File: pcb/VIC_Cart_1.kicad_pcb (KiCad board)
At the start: 2 copper layers, 126.5 x 77.3 mm, 30 parts, among them J1 VIC-20_Expansion_Port, J2 I2C Display, SW1 SW_Push, SW2 SW_Push, SW3 SW_Push, U1 ATMEGA328P-PU, U2 KM681000CLG-5L, U3 M27C160, U4 74LS148, U5 74LS21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

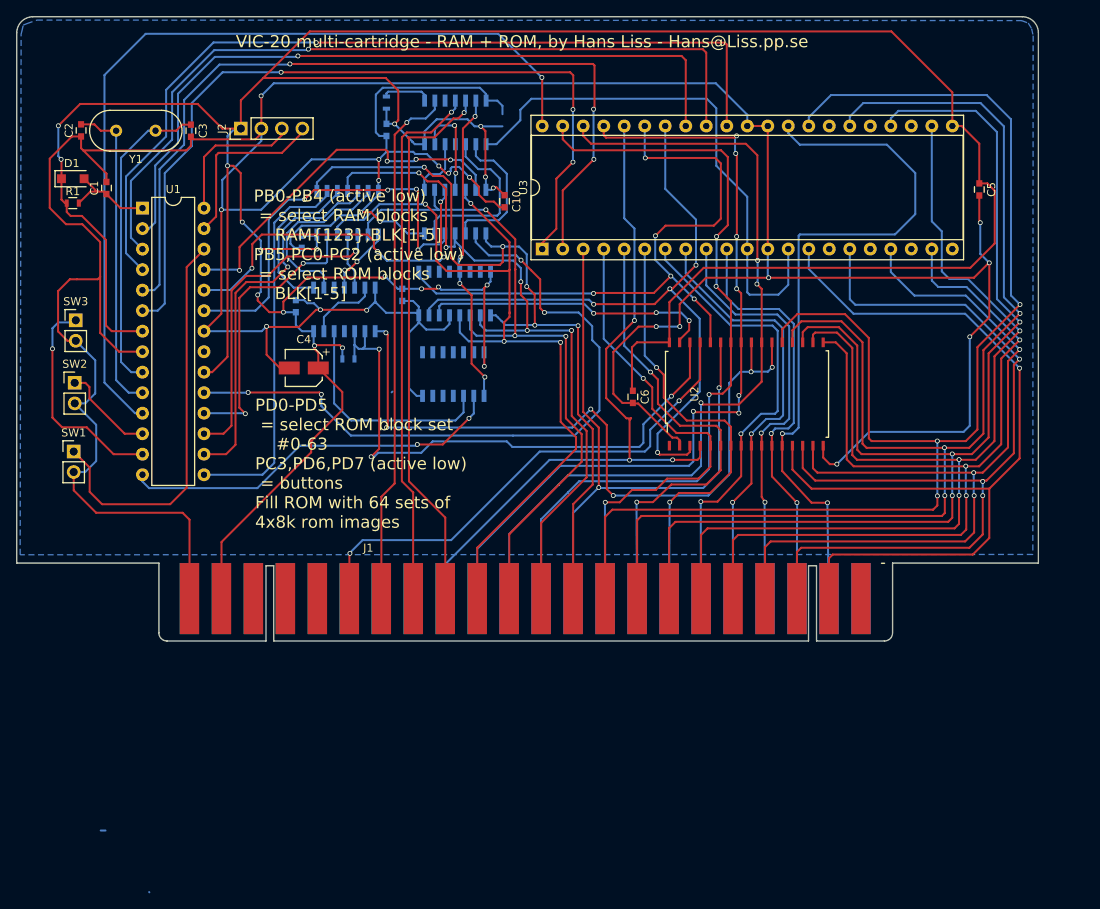
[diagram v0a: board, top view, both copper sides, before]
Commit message: Changed pads to pin header footprint for buttons Inverted BLK inputs to encoder to correct addressing error Added component values to silkscreen
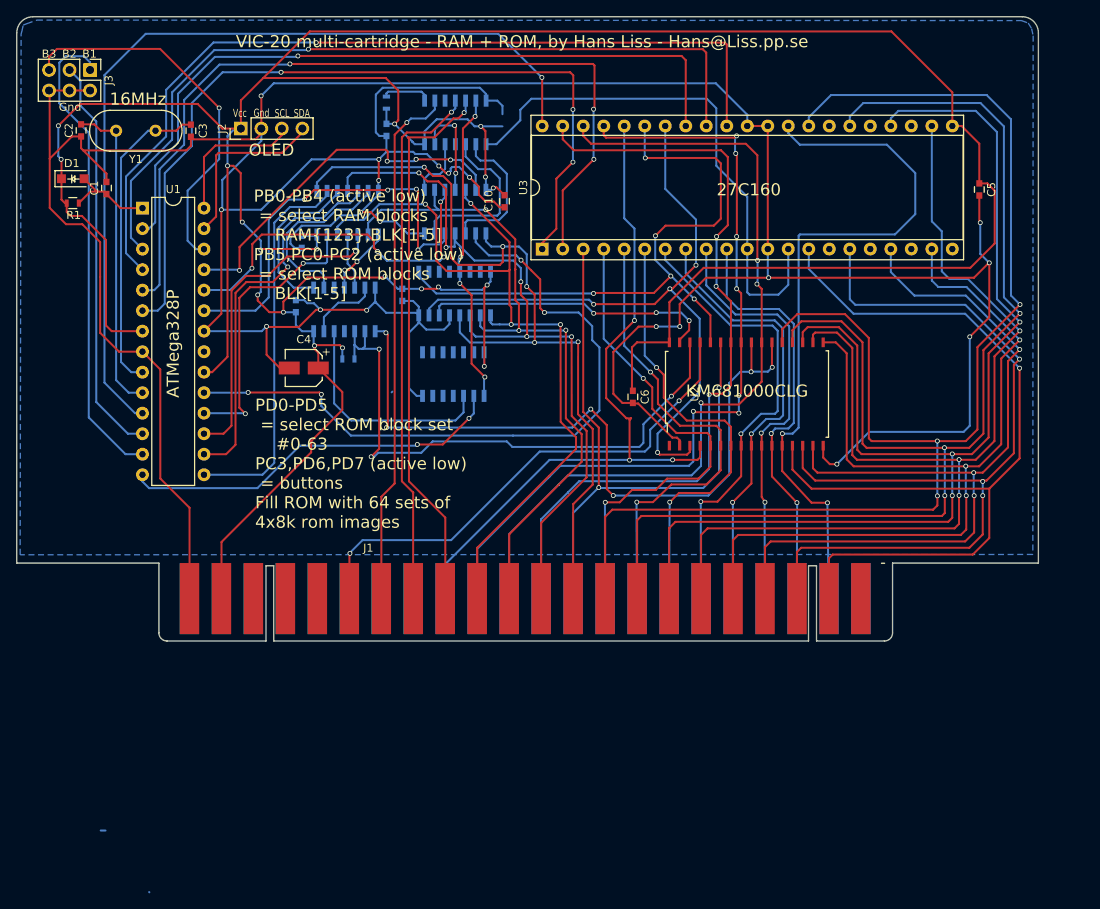
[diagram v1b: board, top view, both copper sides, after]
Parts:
- removed SW1, SW2, SW3: SW_Push, Pin_Headers:Pin_Header_Straight_1x02_Pitch2.54mm
- added J3: Buttons, Pin_Headers:Pin_Header_Straight_2x03_Pitch2.54mm, F.Cu at (53.1, 38.8)
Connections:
- J1 pad 1: Net-(J1-Pad1) -> (no net)
- J1 pad 18: Net-(J1-Pad18) -> (no net)
- J1 pad 19: Net-(J1-Pad19) -> (no net)
- J1 pad 20: Net-(J1-Pad20) -> (no net)
- J1 pad A: Net-(J1-PadA) -> (no net)
- J1 pad S: Net-(J1-PadS) -> (no net)
- J1 pad T: Net-(J1-PadT) -> (no net)
- J1 pad U: Net-(J1-PadU) -> (no net)
- J1 pad V: Net-(J1-PadV) -> (no net)
- J1 pad W: Net-(J1-PadW) -> (no net)
- J1 pad X: Net-(J1-PadX) -> (no net)
- J1 pad Y: Net-(J1-PadY) -> (no net)
- J1 pad Z: Net-(J1-PadZ) -> (no net)
- U1 pad 21: Net-(U1-Pad21) -> (no net)
- U2 pad 1: Net-(U2-Pad1) -> (no net)
- U3 pad 15: Net-(U3-Pad15) -> (no net)
- U3 pad 17: Net-(U3-Pad17) -> (no net)
- U3 pad 19: Net-(U3-Pad19) -> (no net)
- U3 pad 21: Net-(U3-Pad21) -> (no net)
- U3 pad 24: Net-(U3-Pad24) -> (no net)
- U3 pad 26: Net-(U3-Pad26) -> (no net)
- U3 pad 28: Net-(U3-Pad28) -> (no net)
- U4 pad 1: /~BLK1 -> /~BLK5
- U4 pad 10: Net-(U4-Pad10) -> (no net)
- U4 pad 11: Net-(U4-Pad11) -> (no net)
- U4 pad 12: Net-(U4-Pad12) -> (no net)
- U4 pad 14: Net-(U4-Pad14) -> (no net)
- U4 pad 15: Net-(U4-Pad15) -> (no net)
- U4 pad 2: /~BLK2 -> /~BLK3
- U4 pad 3: /~BLK3 -> /~BLK2
- U4 pad 4: /~BLK5 -> /~BLK1
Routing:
- net /~BUTTON2: track 11.8 -> 49.8 mm
- net /~BUTTON3: track 27.4 -> 59.4 mm, vias 1 -> 0
- net GND: track 530.1 -> 513.0 mm
- net /~BLK1: track 100.2 -> 106.2 mm
- net /~BLK5: track 104.3 -> 98.8 mm
- net /~BUTTON1: track 49.7 -> 46.8 mm, vias 0 -> 1
- net /~BLK2: track 92.6 -> 94.6 mm
- net /~BLK3: track 87.7 -> 86.0 mm
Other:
- board text added: "16MHz"
- board text added: "27C160"
- board text added: "74LS148"
- board text added: "74LS21"
- board text added: "74LS32"
- board text added: "ATMega328P"
- board text added: "B1"
- board text added: "B2"
- board text added: "B3"
- board text added: "Gnd"
- board text added: "KM681000CLG"
- board text added: "OLED"
- board text added: "SCL"
- board text added: "SDA"
- board text added: "Vcc"

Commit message: No change
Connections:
- J1 pad X: (no net) -> Net-(J1-PadX)
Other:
- board text added: "555"
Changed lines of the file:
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@@
     (area 43.924999 32.139799 170.615001 109.604881)
     (thickness 1.6)
-    (drawings 54)
-    (tracks 1526)
+    (drawings 55)
+    (tracks 1528)
     (zones 0)
     (modules 28)
-    (nets 73)
+    (nets 74)
   )
   (page A4)
@@
   (net 71 "Net-(U6-Pad13)")
   (net 72 "Net-(U6-Pad12)")
+  (net 73 "Net-(J1-PadX)")
   (net_class Default "This is the default net class."
     (clearance 0.2)
@@
     (add_net "Net-(J1-Pad15)")
     (add_net "Net-(J1-Pad16)")
+    (add_net "Net-(J1-PadX)")
     (add_net "Net-(R2-Pad2)")
     (add_net "Net-(R3-Pad2)")
@@
     (pad Z connect rect (at -83.12726 -0.71888) (size 2.4 8.8) (layers B.Cu B.Mask))
     (pad Y connect rect (at -79.16726 -0.71888) (size 2.4 8.8) (layers B.Cu B.Mask))
-    (pad X connect rect (at -75.20726 -0.71888) (size 2.4 8.8) (layers B.Cu B.Mask))
+    (pad X connect rect (at -75.20726 -0.71888) (size 2.4 8.8) (layers B.Cu B.Mask)
+      (net 73 "Net-(J1-PadX)"))
     (pad W connect rect (at -71.24726 -0.71888) (size 2.4 8.8) (layers B.Cu B.Mask))
     (pad V connect rect (at -67.28726 -0.71888) (size 2.4 8.8) (layers B.Cu B.Mask))
@@
       (rotate (xyz 0 0 0))
     )
+  )
+  (gr_text 555 (at 148.19 38.04 90) (layer B.SilkS)
+    (effects (font (size 1.5 1.5) (thickness 0.3)) (justify mirror))
   )
   (gr_line (start 50.82 52.32) (end 50.31 52.32) (angle 90) (layer F.SilkS) (width 0.05))
@@
   (segment (start 80.29956 34.03092) (end 74.53122 39.79926) (width 0.25) (layer F.Cu) (net 23))
   (segment (start 74.53122 39.79926) (end 71.755 42.57548) (width 0.25) (layer F.Cu) (net 23))
-  (segment (start 152.32888 34.03092) (end 80.29956 34.03092) (width 0.25) (layer F.Cu) (net 23))
-  (segment (start 159.8803 41.58234) (end 152.32888 34.03092) (width 0.25) (layer F.Cu) (net 23))
+  (segment (start 152.32888 34.03092) (end 145.29 34.03092) (width 0.25) (layer F.Cu) (net 23))
+  (segment (start 145.29 34.03092) (end 80.29956 34.03092) (width 0.25) (layer F.Cu) (net 23))
+  (segment (start 159.8803 41.58234) (end 152.85398 34.55602) (width 0.25) (layer F.Cu) (net 23))
+  (segment (start 152.85398 34.55602) (end 152.32888 34.03092) (width 0.25) (layer F.Cu) (net 23))
   (segment (start 79.2988 59.3464) (end 79.04156 59.3464) (width 0.25) (layer B.Cu) (net 23) (status 30))
   (segment (start 67.19062 76.2381) (end 68.199 76.2381) (width 0.25) (layer F.Cu) (net 23))

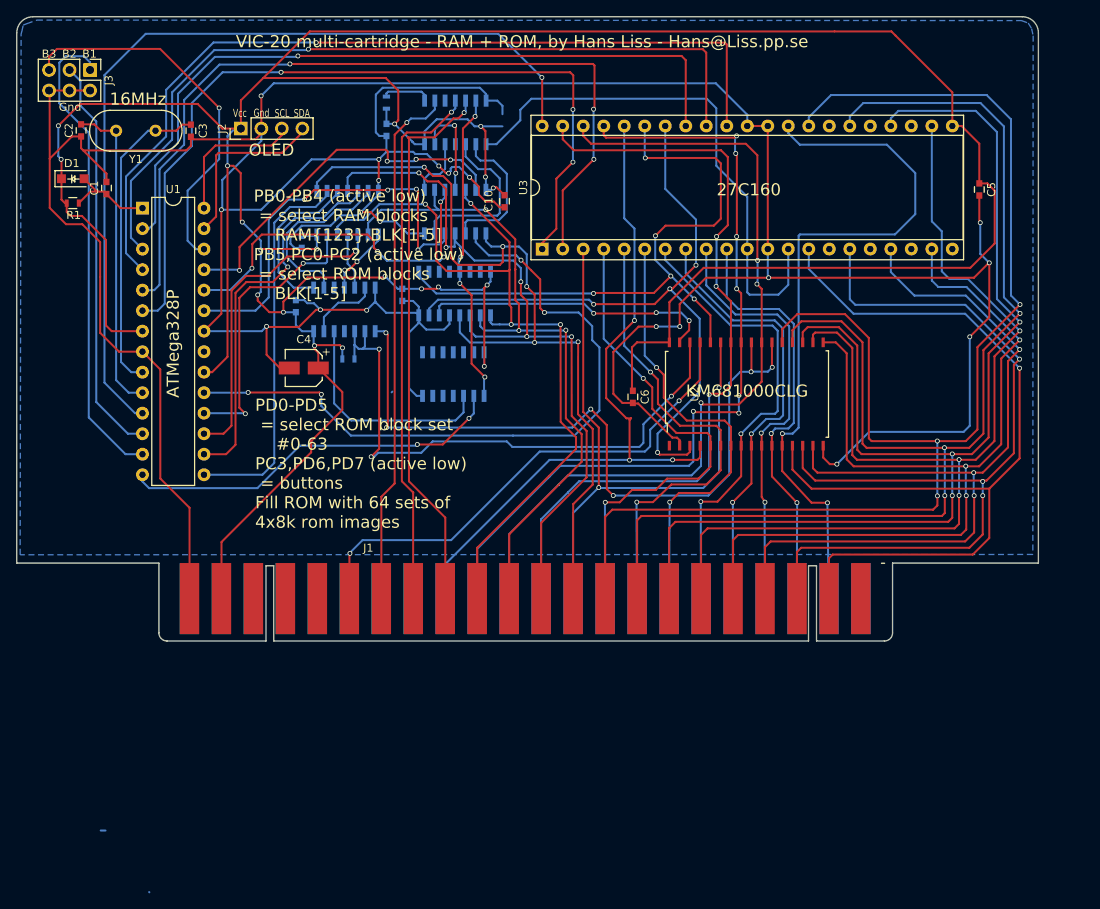
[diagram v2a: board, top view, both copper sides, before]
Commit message: Added mounting hole Added title
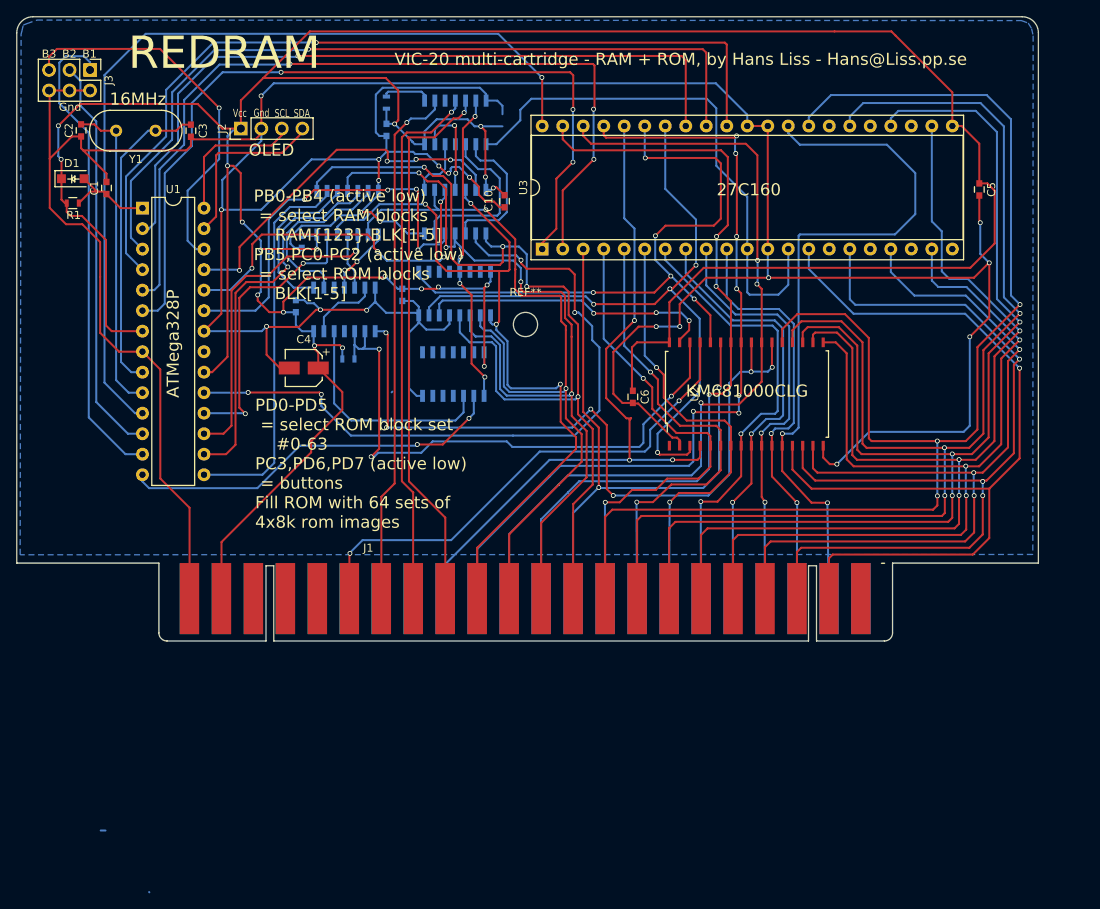
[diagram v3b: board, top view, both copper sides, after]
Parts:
- added REF**: MountingHole_3mm, Mounting_Holes:MountingHole_3mm, F.Cu at (107.0, 70.3)
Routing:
- net /~BLK3: track 86.0 -> 97.7 mm, vias 3 -> 2
- net /~BLK2: track 94.6 -> 106.0 mm, vias 5 -> 4
- net /~BLK1: track 106.2 -> 117.3 mm, vias 5 -> 4
- net /~SEL_ROM_BLK1: track 86.2 -> 87.1 mm
- net BA2: track 36.3 -> 36.9 mm
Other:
- board text added: "REDRAM"
- board text removed: "555"

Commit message: Moved button pin header to the right Changed outline to match existing (large) carts, e.g. 16k expansion
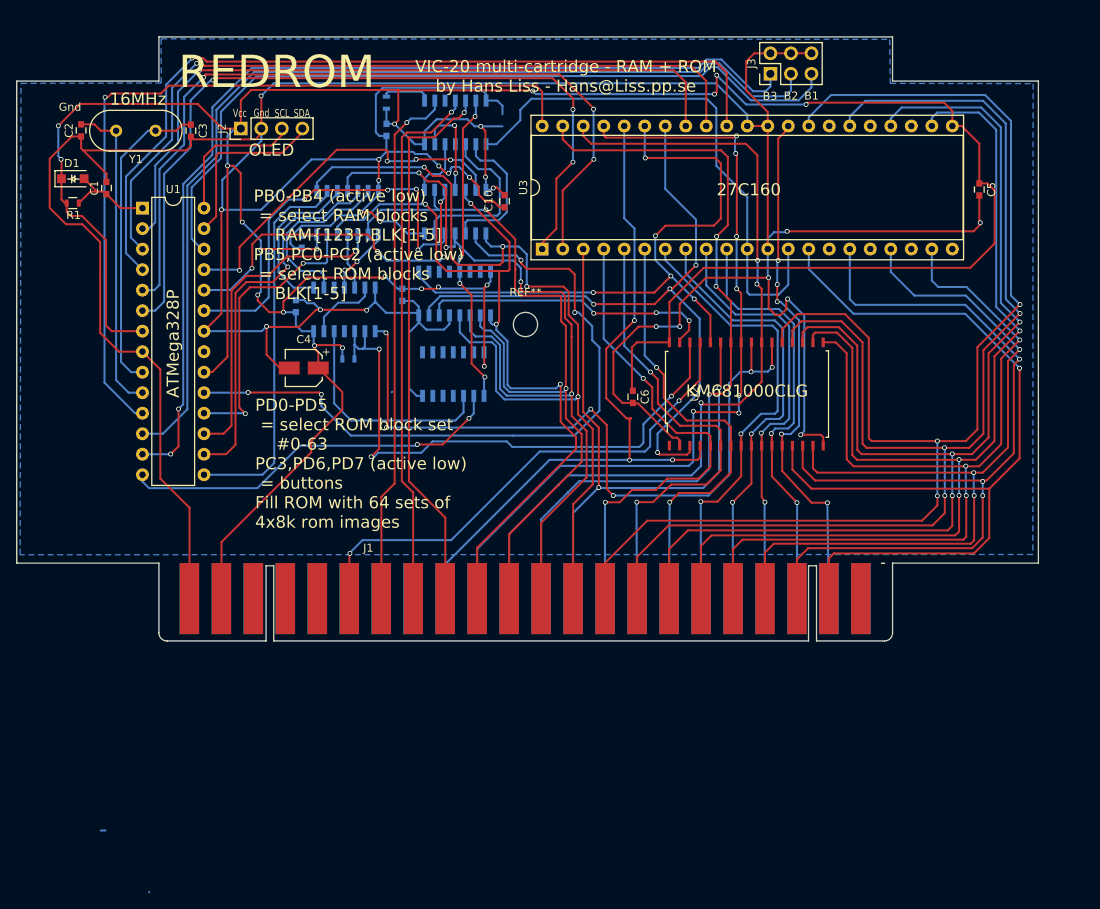
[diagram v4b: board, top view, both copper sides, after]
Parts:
- moved J3 84.3 mm to (137.3, 39.3), turned to 90 degrees
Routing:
- net /~BUTTON2: track 49.8 -> 123.0 mm
- net /~BUTTON3: track 59.4 -> 123.6 mm, vias 0 -> 2
- net /~BUTTON1: track 46.8 -> 98.9 mm, vias 1 -> 0
- net A0: track 89.2 -> 65.5 mm, vias 2 -> 5
- net VCC: track 450.4 -> 429.3 mm, vias 19 -> 23
- net GND: track 513.0 -> 498.8 mm
- net RB5: track 109.0 -> 101.2 mm
- net D4: track 133.8 -> 138.2 mm
- net RB3: track 104.2 -> 100.6 mm
- net D7: track 170.5 -> 167.1 mm
- net RB1: track 100.3 -> 97.1 mm
- net RB2: track 107.6 -> 104.4 mm
- net RB0: track 92.7 -> 89.7 mm
- net RB4: track 101.4 -> 99.3 mm
- net D6: track 159.8 -> 157.7 mm
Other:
- board size 126.5 x 77.3 mm -> 126.5 x 74.8 mm
- board text added: "REDROM"
- board text added: "VIC-20 multi-cartridge - RAM + ROM by Hans Liss - Hans@Liss.pp.se"
- board text removed: "REDRAM"
- board text removed: "VIC-20 multi-cartridge - RAM + ROM, by Hans Liss - Hans@Liss.pp.se"

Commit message: Changed silkscreen text
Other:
- board text added: "VIC-20 ROM + RAM cartridge by Hans Liss - Hans@Liss.pp.se"
- board text removed: "VIC-20 multi-cartridge - RAM + ROM by Hans Liss - Hans@Liss.pp.se"
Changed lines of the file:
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@@
     (effects (font (size 1.5 1.5) (thickness 0.3)) (justify left))
   )
-  (gr_text "VIC-20 multi-cartridge - RAM + ROM\nby Hans Liss - Hans@Liss.pp.se" (at 112.01 39.59) (layer F.SilkS)
+  (gr_text "VIC-20 ROM + RAM cartridge\nby Hans Liss - Hans@Liss.pp.se" (at 112.01 39.59) (layer F.SilkS)
     (effects (font (size 1.5 1.5) (thickness 0.3)))
   )

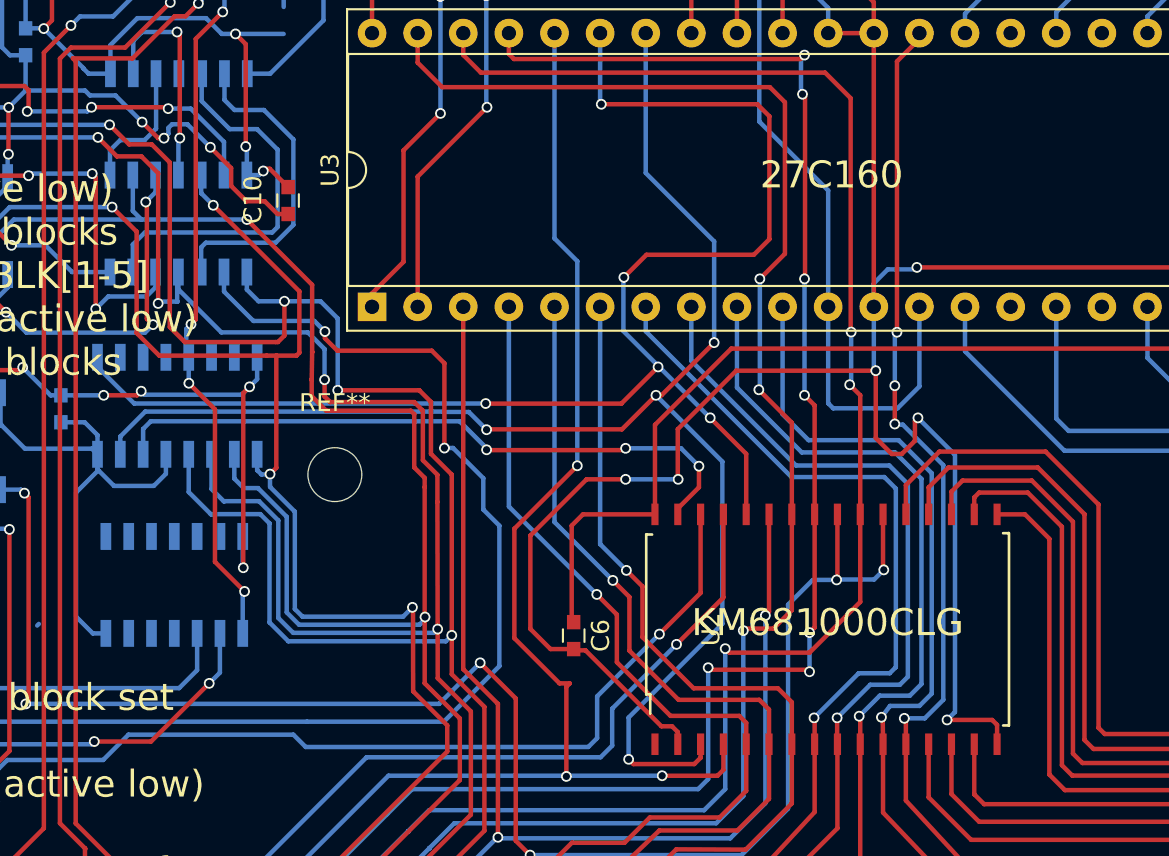
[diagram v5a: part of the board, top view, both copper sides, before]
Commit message: Moved capacitor to back Grounded A17, A18 for 512k RAM Added RAM chip to project lib
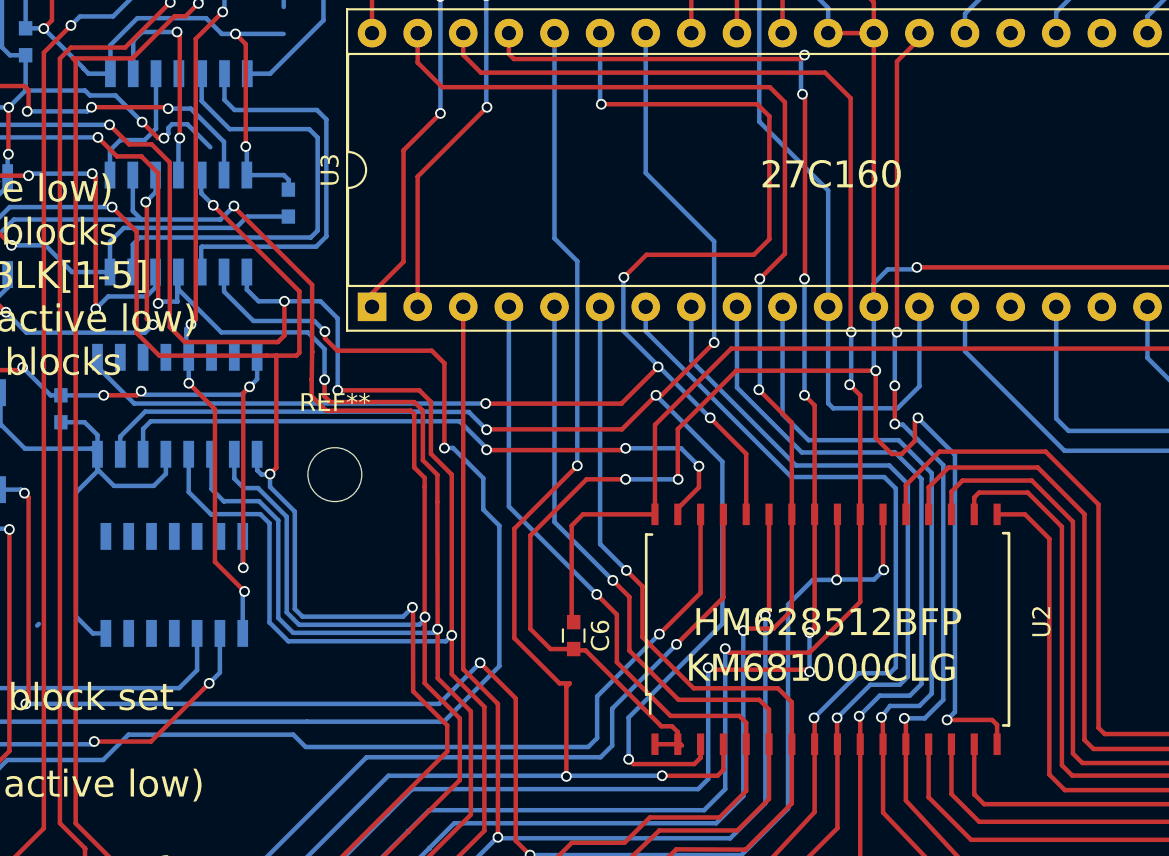
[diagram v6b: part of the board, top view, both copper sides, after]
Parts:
- C10: moved to B.Cu
- U2: value KM681000CLG-5L -> HM628512BFP-5
- moved C10 0.14 mm to (104.4, 55.2)
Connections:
- J1 pad X: Net-(J1-PadX) -> (no net)
- U2 pad 1: (no net) -> GND
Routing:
- net GND: track 498.8 -> 506.1 mm, vias 19 -> 18
- net Net-(U5-Pad10): track 21.2 -> 26.2 mm
- net Net-(U5-Pad9): track 18.0 -> 22.7 mm
- net /~BLK3: track 97.7 -> 98.4 mm
- net VCC: track 429.3 -> 429.5 mm, vias 23 -> 22
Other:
- board text added: "HM628512BFP"
